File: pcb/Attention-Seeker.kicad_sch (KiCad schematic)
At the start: 21 parts, among them Q1 BSS84, SW1 RotaryEncoder_Switch, SW2 SW_Push, SW3 SW_Push, SW4 SW_Push, U1 TFT_320x240, U2 ESP32-S3-DevKitC, U3 IRLML2502TRPBF, U4 AMS1117-3.3

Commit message: updated rotary encoder footprint and sourced smd parts from other source
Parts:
- SW1: footprint Rotary_Encoder:RotaryEncoder_Alps_EC12E-Switch_Vertical_H20mm -> Rotary_Encoder:RotaryEncoder_Alps_EC11E-Switch_Vertical_H20mm
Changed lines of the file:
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@@
 			)
 		)
-		(property "Footprint" "Rotary_Encoder:RotaryEncoder_Alps_EC12E-Switch_Vertical_H20mm"
+		(property "Footprint" "Rotary_Encoder:RotaryEncoder_Alps_EC11E-Switch_Vertical_H20mm"
 			(at 135.89 89.916 0)
 			(effects

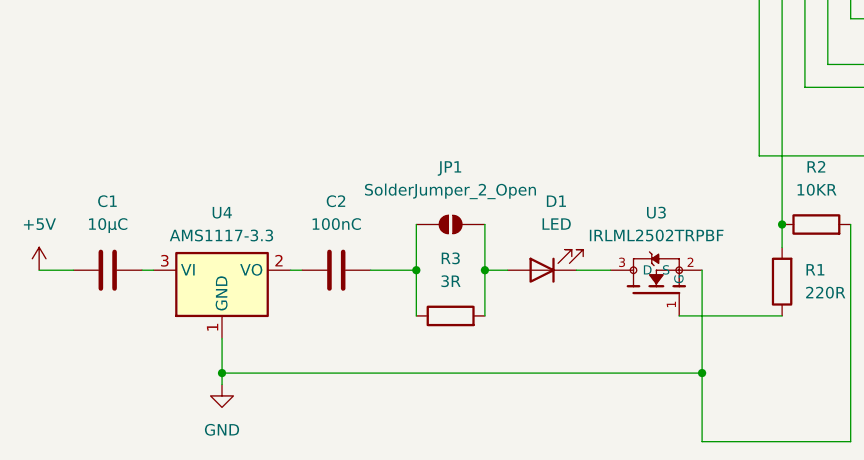
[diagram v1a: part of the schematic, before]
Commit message: fixed critical issue with cap alignment
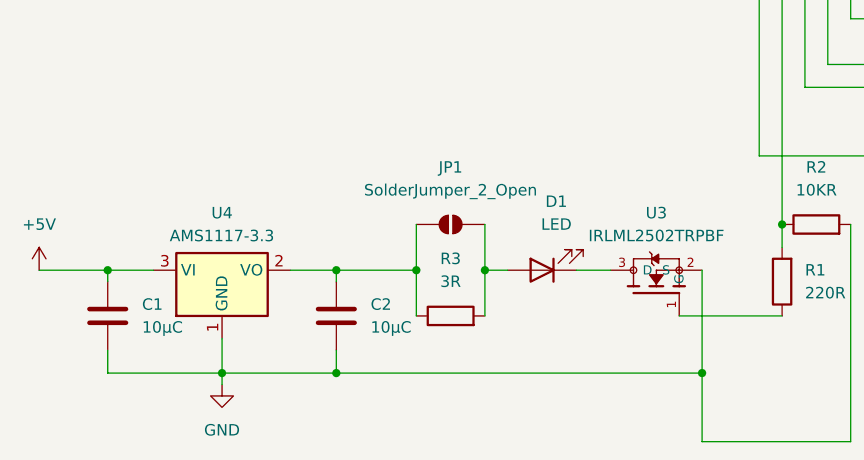
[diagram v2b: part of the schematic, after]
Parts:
- C2: value 100nC -> 10µC
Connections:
- net +5V: now also C1.2, U4.3 (VI); no longer C1.1
- net GND: now also C1.1, C2.1
- net at C2.2, JP1.1 (A), R3.1: now also U4.2 (VO)
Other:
- moved on the sheet: C1, C2
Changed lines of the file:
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@@
 	)
 	(junction
+		(at 49.53 161.29)
+		(diameter 0)
+		(color 0 0 0 0)
+	)
+	(junction
+		(at 49.53 172.72)
+		(diameter 0)
+		(color 0 0 0 0)
+	)
+	(junction
 		(at 99.06 156.21)
 		(diameter 0)
@@
 	)
 	(junction
+		(at 24.13 161.29)
+		(diameter 0)
+		(color 0 0 0 0)
+	)
+	(junction
 		(at 142.24 48.26)
 		(diameter 0)
@@
 	(wire
 		(pts
-			(xy 53.34 161.29) (xy 58.42 161.29)
-		)
-		(stroke
-			(width 0)
-			(type default)
-		)
-	)
-	(wire
-		(pts
 			(xy 58.42 156.21) (xy 58.42 161.29)
 		)
@@
 	(wire
 		(pts
-			(xy 85.09 25.4) (xy 85.09 59.69)
+			(xy 24.13 161.29) (xy 29.21 161.29)
 		)
 		(stroke
@@
 	(wire
 		(pts
-			(xy 128.27 93.98) (xy 132.08 93.98)
+			(xy 85.09 25.4) (xy 85.09 59.69)
 		)
 		(stroke
@@
 	(wire
 		(pts
-			(xy 165.1 57.15) (xy 172.72 57.15)
+			(xy 128.27 93.98) (xy 132.08 93.98)
 		)
 		(stroke
@@
 	(wire
 		(pts
-			(xy 176.53 138.43) (xy 180.34 138.43)
+			(xy 165.1 57.15) (xy 172.72 57.15)
 		)
 		(stroke
@@
 	(wire
 		(pts
-			(xy 144.78 158.75) (xy 147.32 158.75)
+			(xy 176.53 138.43) (xy 180.34 138.43)
 		)
 		(stroke
@@
 	(wire
 		(pts
-			(xy 27.94 161.29) (xy 29.21 161.29)
+			(xy 144.78 158.75) (xy 147.32 158.75)
 		)
 		(stroke
@@
 	(wire
 		(pts
+			(xy 49.53 161.29) (xy 58.42 161.29)
+		)
+		(stroke
+			(width 0)
+			(type default)
+		)
+	)
+	(wire
+		(pts
 			(xy 165.1 46.99) (xy 175.26 46.99)
 		)
@@
 	(wire
 		(pts
-			(xy 36.83 172.72) (xy 90.17 172.72)
+			(xy 24.13 172.72) (xy 36.83 172.72)
+		)
+		(stroke
+			(width 0)
+			(type default)
+		)
+	)
+	(wire
+		(pts
+			(xy 36.83 172.72) (xy 49.53 172.72)
+		)
+		(stroke
+			(width 0)
+			(type default)
+		)
+	)
+	(wire
+		(pts
+			(xy 49.53 161.29) (xy 49.53 162.56)
 		)
 		(stroke
@@
 	(wire
 		(pts
+			(xy 24.13 170.18) (xy 24.13 172.72)
+		)
+		(stroke
+			(width 0)
+			(type default)
+		)
+	)
+	(wire
+		(pts
 			(xy 168.91 138.43) (xy 168.91 135.89)
 		)
@@
 	(wire
 		(pts
+			(xy 49.53 172.72) (xy 90.17 172.72)
+		)
+		(stroke
+			(width 0)
+			(type default)
+		)
+	)
+	(wire
+		(pts
 			(xy 36.83 168.91) (xy 36.83 172.72)
 		)
@@
 	(wire
 		(pts
+			(xy 49.53 170.18) (xy 49.53 172.72)
+		)
+		(stroke
+			(width 0)
+			(type default)
+		)
+	)
+	(wire
+		(pts
 			(xy 66.04 161.29) (xy 66.04 166.37)
 		)
@@
 	(wire
 		(pts
-			(xy 44.45 161.29) (xy 45.72 161.29)
+			(xy 44.45 161.29) (xy 49.53 161.29)
 		)
 		(stroke
@@
 	(wire
 		(pts
+			(xy 24.13 161.29) (xy 24.13 162.56)
+		)
+		(stroke
+			(width 0)
+			(type default)
+		)
+	)
+	(wire
+		(pts
 			(xy 175.26 57.15) (xy 172.72 57.15)
 		)
@@
 	(wire
 		(pts
-			(xy 16.51 161.29) (xy 20.32 161.29)
+			(xy 16.51 161.29) (xy 24.13 161.29)
 		)
 		(stroke
@@
 	(symbol
 		(lib_id "Device:C")
-		(at 24.13 161.29 90)
+		(at 24.13 166.37 180)
 		(unit 1)
 		(exclude_from_sim no)
@@
 		(fields_autoplaced yes)
 		(property "Reference" "C1"
-			(at 24.13 153.67 90)
+			(at 27.94 165.0999 0)
 			(effects
 				(font
 					(size 1.27 1.27)
 				)
+				(justify right)
 			)
 		)
 		(property "Value" "10µC"
-			(at 24.13 156.21 90)
+			(at 27.94 167.6399 0)
 			(effects
 				(font
 					(size 1.27 1.27)
 				)
+				(justify right)
 			)
 		)
 		(property "Footprint" "Capacitor_SMD:C_1206_3216Metric_Pad1.33x1.80mm_HandSolder"
-			(at 27.94 160.3248 0)
+			(at 23.1648 162.56 0)
 			(effects
 				(font
@@
 		)
 		(property "Datasheet" "~"
-			(at 24.13 161.29 0)
+			(at 24.13 166.37 0)
 			(effects
 				(font
@@
 		)
 		(property "Description" "Unpolarized capacitor"
-			(at 24.13 161.29 0)
+			(at 24.13 166.37 0)
 			(effects
 				(font
@@
 		)
 		(instances
-			(project ""
+			(project "Attention-Seeker"
 				(path "/684e7490-c2ec-4c8f-b0cc-1cb7d98f4c0d"
 					(reference "C1")
@@
 	(symbol
 		(lib_id "Device:C")
-		(at 49.53 161.29 90)
+		(at 49.53 166.37 180)
 		(unit 1)
 		(exclude_from_sim no)
@@
 		(fields_autoplaced yes)
 		(property "Reference" "C2"
-			(at 49.53 153.67 90)
+			(at 53.34 165.0999 0)
 			(effects
 				(font
 					(size 1.27 1.27)
 				)
+				(justify right)
 			)
 		)
-		(property "Value" "100nC"
-			(at 49.53 156.21 90)
+		(property "Value" "10µC"
+			(at 53.34 167.6399 0)
 			(effects
 				(font
 					(size 1.27 1.27)
 				)
+				(justify right)
 			)
 		)
 		(property "Footprint" "Capacitor_SMD:C_1206_3216Metric_Pad1.33x1.80mm_HandSolder"
-			(at 53.34 160.3248 0)
+			(at 48.5648 162.56 0)
 			(effects
 				(font
@@
 		)
 		(property "Datasheet" "~"
-			(at 49.53 161.29 0)
+			(at 49.53 166.37 0)
 			(effects
 				(font
@@
 		)
 		(property "Description" "Unpolarized capacitor"
-			(at 49.53 161.29 0)
+			(at 49.53 166.37 0)
 			(effects
 				(font
